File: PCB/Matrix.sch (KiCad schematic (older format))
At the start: 167 parts

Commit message: PCB update
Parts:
- added MX?: 6U, MX_Solder_SawnsProjects:MXOnly-6U-ReversedStabilizers-NoLED, symbol random-keyboard-parts:MX-NoLED-MX_Alps_Hybrid
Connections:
- net at RGB9.2 (DOUT): now also RGB18.4 (DIN)
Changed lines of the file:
@@
 	5150 4550 5150 4600
 Connection ~ 5150 4550
+Wire Wire Line
+	10400 6600 10850 6600
+Wire Wire Line
+	10850 6600 10850 5750
+$Comp
+L random-keyboard-parts:MX-NoLED-MX_Alps_Hybrid MX?
+U 1 1 6342F4CC
+P 3500 4375
+F 0 "MX?" H 3533 4584 39  0000 C CNN
+F 1 "6U" H 3533 4525 20  0000 C CNN
+F 2 "MX_Solder_SawnsProjects:MXOnly-6U-ReversedStabilizers-NoLED" H 2875 4350 60  0001 C CNN
+F 3 "" H 2875 4350 60  0001 C CNN
+	1    3500 4375
+	1    0    0    -1
+$EndComp
 $EndSCHEMATC

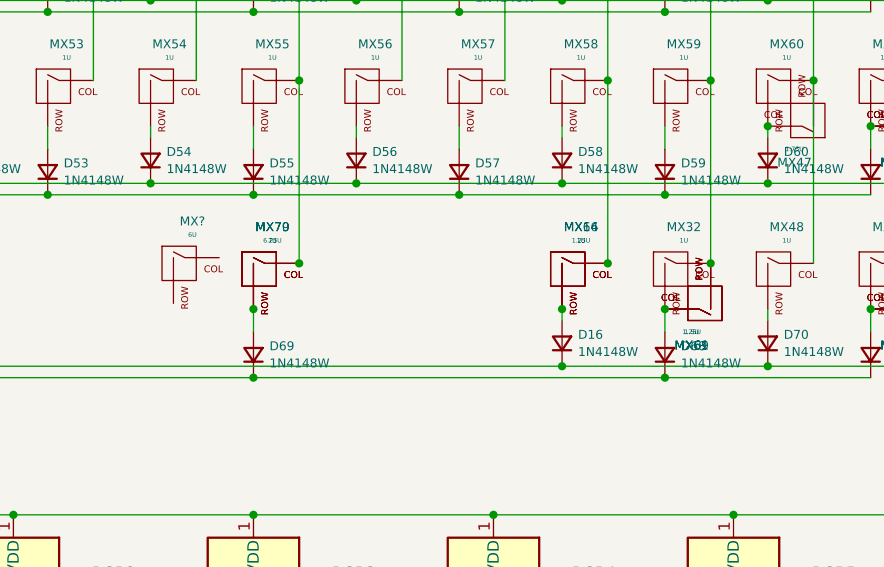
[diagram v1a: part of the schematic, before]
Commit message: Fix PCB error, Add keyswitch for 6U Spacebar PCB
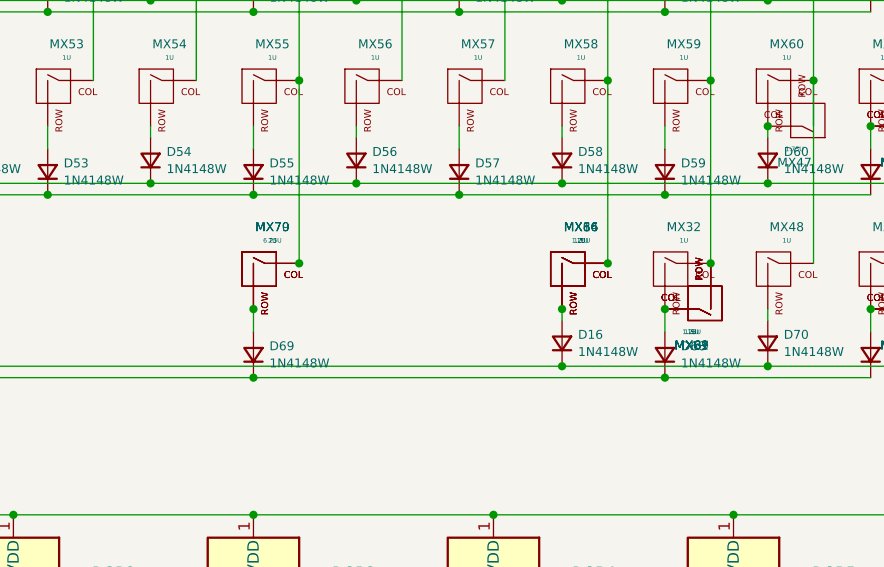
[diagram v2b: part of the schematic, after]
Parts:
- removed MX?: 6U, MX_Solder_SawnsProjects:MXOnly-6U-ReversedStabilizers-NoLED, symbol random-keyboard-parts:MX-NoLED-MX_Alps_Hybrid
- added MX86: 1.5U, MX_Solder_SawnsProjects:MXOnly-1.5U-NoLED, symbol random-keyboard-parts:MX-NoLED-MX_Alps_Hybrid
- added MX87: 1U, MX_Solder_SawnsProjects:MXOnly-1U-NoLED, symbol random-keyboard-parts:MX-NoLED-MX_Alps_Hybrid
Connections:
- net C4: now also MX86.1 (COL)
- net C5: now also MX87.2 (ROW)
- net at D68.2 (A), MX32.2 (ROW), MX61.1 (COL)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: now also MX87.1 (COL)
- net at D16.2 (A), MX16.2 (ROW), MX64.2 (ROW): now also MX86.2 (ROW)
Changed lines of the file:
@@
 	10850 6600 10850 5750
 $Comp
-L random-keyboard-parts:MX-NoLED-MX_Alps_Hybrid MX?
-U 1 1 6342F4CC
-P 3500 4375
-F 0 "MX?" H 3533 4584 39  0000 C CNN
-F 1 "6U" H 3533 4525 20  0000 C CNN
-F 2 "MX_Solder_SawnsProjects:MXOnly-6U-ReversedStabilizers-NoLED" H 2875 4350 60  0001 C CNN
-F 3 "" H 2875 4350 60  0001 C CNN
-	1    3500 4375
+L random-keyboard-parts:MX-NoLED-MX_Alps_Hybrid MX86
+U 1 1 634438A3
+P 5200 4400
+F 0 "MX86" H 5233 4609 39  0000 C CNN
+F 1 "1.5U" H 5233 4550 20  0000 C CNN
+F 2 "MX_Solder_SawnsProjects:MXOnly-1.5U-NoLED" H 4575 4375 60  0001 C CNN
+F 3 "" H 4575 4375 60  0001 C CNN
+	1    5200 4400
 	1    0    0    -1
 $EndComp
+$Comp
+L random-keyboard-parts:MX-NoLED-MX_Alps_Hybrid MX87
+U 1 1 6345B4A9
+P 5750 4500
+F 0 "MX87" H 5783 4709 39  0000 C CNN
+F 1 "1U" H 5783 4650 20  0000 C CNN
+F 2 "MX_Solder_SawnsProjects:MXOnly-1U-NoLED" H 5125 4475 60  0001 C CNN
+F 3 "" H 5125 4475 60  0001 C CNN
+	1    5750 4500
+	-1   0    0    1
+$EndComp
 $EndSCHEMATC
